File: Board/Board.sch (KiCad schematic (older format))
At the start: 55 parts, among them J1 Screw_Terminal_1x02, P1 USB_B, P2 CONN_01X05, P3 CONN_01X06, SW1 SW_SPST, SW2 SW_SPST, U1 MCP23016, U2 LM1117-3.3, U3 MCP9808, U4 ESP-12E

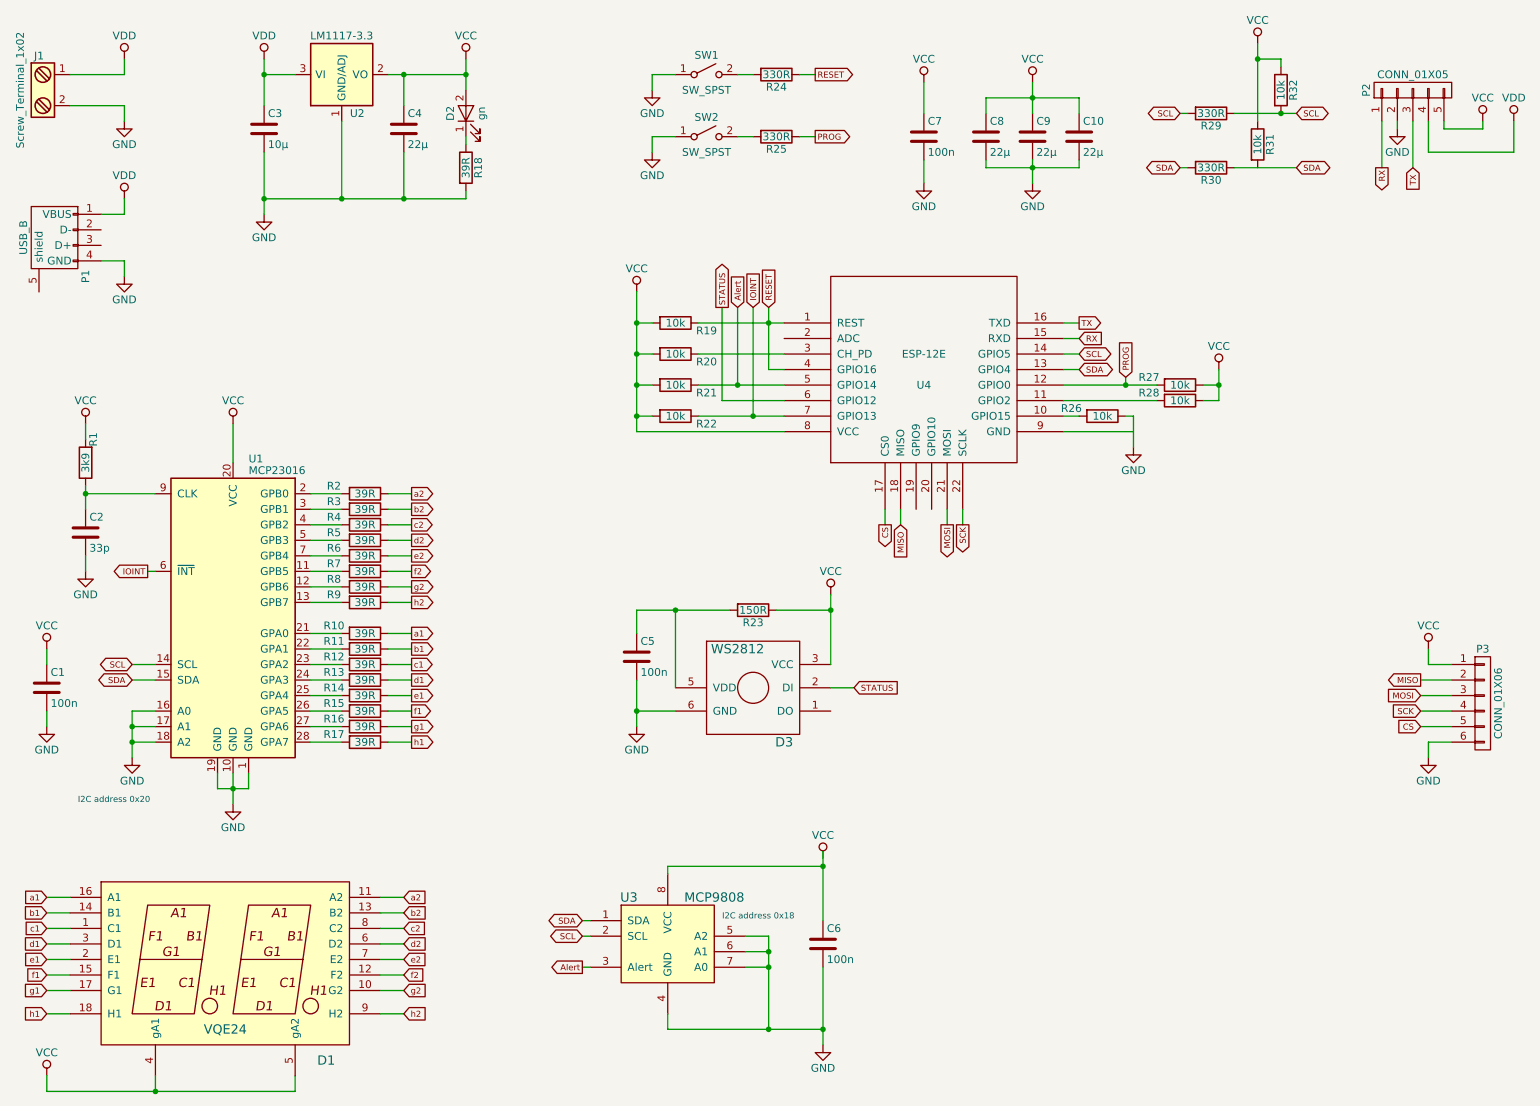
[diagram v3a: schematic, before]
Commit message: Layout for power and 7 segment display
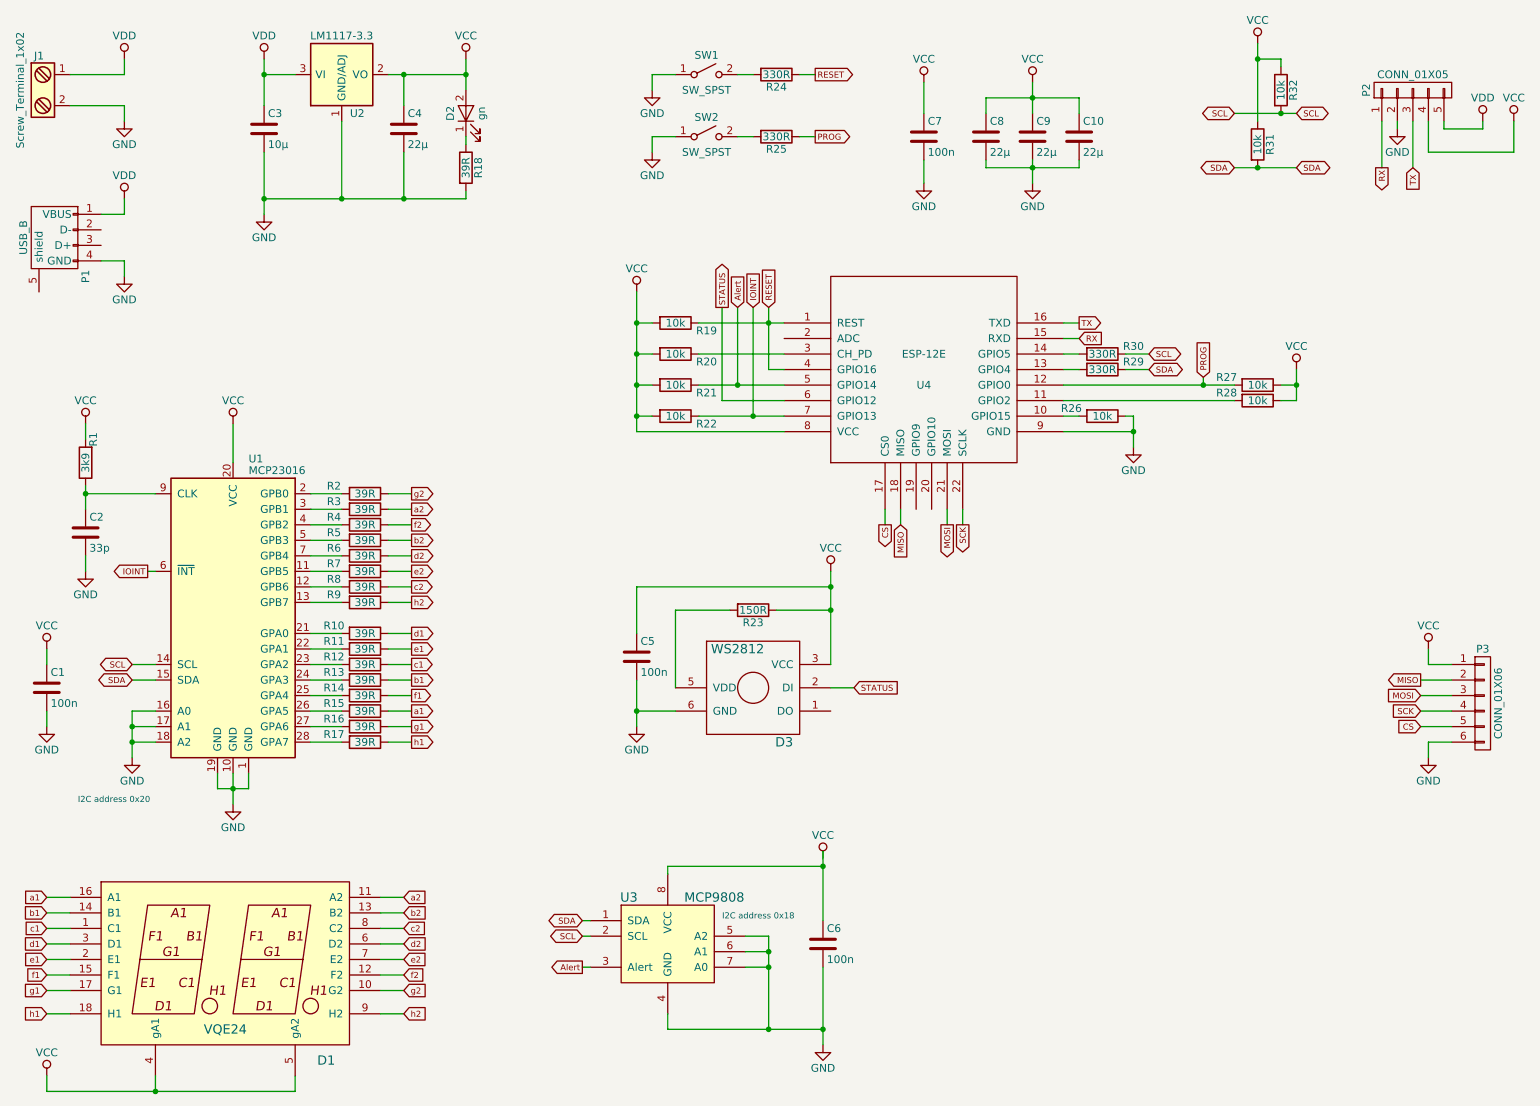
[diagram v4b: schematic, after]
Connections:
- net GND: now also U4.9 (GND)
- net SCL: now also R30.1; no longer R29.1, R29.2, U4.14 (GPIO5)
- net SDA: now also R29.1, R31.2; no longer R30.1, R30.2, U4.13 (GPIO4)
- net VCC: now also C5.1, P2.4 (P4); no longer P2.5 (P5)
- net VDD: now also P2.5 (P5); no longer P2.4 (P4)
- net a1: now also R15.1; no longer R10.1
- net a2: now also R3.1; no longer R2.1
- net b1: now also R13.1; no longer R11.1
- net b2: now also R5.1; no longer R3.1
- net c2: now also R8.1; no longer R4.1
- net d1: now also R10.1; no longer R13.1
- net d2: now also R6.1; no longer R5.1
- net e1: now also R11.1; no longer R14.1
- net e2: now also R7.1; no longer R6.1
- net f1: now also R14.1; no longer R15.1
- net f2: now also R4.1; no longer R7.1
- net g2: now also R2.1; no longer R8.1
- net at D3.5 (VDD), R23.2: no longer C5.1
- new net: R29.2, U4.13 (GPIO4)
- new net: R30.2, U4.14 (GPIO5)
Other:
- moved on the sheet: R27, R28, R29, R30

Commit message: Layout rev 1
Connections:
- net CS: now also P3.2 (P2); no longer P3.5 (P5)
- net MISO: now also P3.3 (P3); no longer P3.2 (P2)
- net MOSI: now also P3.4 (P4); no longer P3.3 (P3)
- net RX: now also P2.3 (P3); no longer P2.1 (P1)
- net SCK: now also P3.5 (P5); no longer P3.4 (P4)
- net TX: now also P2.1 (P1); no longer P2.3 (P3)
- net VCC: now also C6.1, U3.8 (VCC)
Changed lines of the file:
@@
 L VCC #PWR03
 U 1 1 5AD1E585
-P 6150 6050
-F 0 "#PWR03" H 6150 5900 50  0001 C CNN
-F 1 "VCC" H 6150 6200 50  0000 C CNN
-F 2 "" H 6150 6050 50  0000 C CNN
-F 3 "" H 6150 6050 50  0000 C CNN
-	1    6150 6050
+P 6150 6000
+F 0 "#PWR03" H 6150 5850 50  0001 C CNN
+F 1 "VCC" H 6150 6150 50  0000 C CNN
+F 2 "" H 6150 6000 50  0000 C CNN
+F 3 "" H 6150 6000 50  0000 C CNN
+	1    6150 6000
 	1    0    0    -1
 $EndComp
@@
 Wire Wire Line
 	5350 3000 5900 3000
-Text GLabel 9750 1600 3    39   Output ~ 0
+Text GLabel 9950 1600 3    39   Output ~ 0
 RX
 Text GLabel 7800 2700 2    39   Input ~ 0
@@
 Text GLabel 7800 2600 2    39   Output ~ 0
 TX
-Text GLabel 9950 1600 3    39   Input ~ 0
+Text GLabel 9750 1600 3    39   Input ~ 0
 TX
 Wire Wire Line
@@
 Wire Wire Line
 	10050 5300 10200 5300
-Text GLabel 10000 4900 0    39   Output ~ 0
+Text GLabel 10000 5000 0    39   Output ~ 0
 MISO
-Text GLabel 10000 5000 0    39   Input ~ 0
+Text GLabel 10000 5100 0    39   Input ~ 0
 MOSI
-Text GLabel 10000 5100 0    39   Input ~ 0
+Text GLabel 10000 5200 0    39   Input ~ 0
 SCK
 Wire Wire Line
@@
 	1    0    0    -1
 $EndComp
-Text GLabel 10000 5200 0    39   Input ~ 0
+Text GLabel 10000 4900 0    39   Input ~ 0
 CS
 Wire Wire Line

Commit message: Final Rev 1
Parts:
- removed C7: 100n, Capacitors_SMD:C_0603_HandSoldering, symbol C
- renumbered C10 to C7
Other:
- moved on the sheet: C7, C8, C9
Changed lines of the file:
@@
 L C C8
 U 1 1 5AD74D33
-P 7200 1400
-F 0 "C8" H 7225 1500 50  0000 L CNN
-F 1 "22µ" H 7225 1300 50  0000 L CNN
-F 2 "Capacitors_SMD:C_1206_HandSoldering" H 7238 1250 50  0001 C CNN
-F 3 "" H 7200 1400 50  0000 C CNN
-	1    7200 1400
-	1    0    0    -1
-$EndComp
-$Comp
-L C C9
-U 1 1 5AD7515D
 P 7500 1400
-F 0 "C9" H 7525 1500 50  0000 L CNN
+F 0 "C8" H 7525 1500 50  0000 L CNN
 F 1 "22µ" H 7525 1300 50  0000 L CNN
 F 2 "Capacitors_SMD:C_1206_HandSoldering" H 7538 1250 50  0001 C CNN
@@
 $EndComp
 $Comp
-L C C10
-U 1 1 5AD7521C
+L C C9
+U 1 1 5AD7515D
 P 7800 1400
-F 0 "C10" H 7825 1500 50  0000 L CNN
+F 0 "C9" H 7825 1500 50  0000 L CNN
 F 1 "22µ" H 7825 1300 50  0000 L CNN
 F 2 "Capacitors_SMD:C_1206_HandSoldering" H 7838 1250 50  0001 C CNN
 F 3 "" H 7800 1400 50  0000 C CNN
 	1    7800 1400
+	1    0    0    -1
+$EndComp
+$Comp
+L C C7
+U 1 1 5AD7521C
+P 7200 1400
+F 0 "C7" H 7225 1500 50  0000 L CNN
+F 1 "22µ" H 7225 1300 50  0000 L CNN
+F 2 "Capacitors_SMD:C_1206_HandSoldering" H 7238 1250 50  0001 C CNN
+F 3 "" H 7200 1400 50  0000 C CNN
+	1    7200 1400
 	1    0    0    -1
 $EndComp
@@
 Wire Wire Line
 	5500 3100 5900 3100
-$Comp
-L C C7
-U 1 1 5AD7760E
-P 6800 1400
-F 0 "C7" H 6825 1500 50  0000 L CNN
-F 1 "100n" H 6825 1300 50  0000 L CNN
-F 2 "Capacitors_SMD:C_0603_HandSoldering" H 6838 1250 50  0001 C CNN
-F 3 "" H 6800 1400 50  0000 C CNN
-	1    6800 1400
-	1    0    0    -1
-$EndComp
-Wire Wire Line
-	6800 1250 6800 1050
-Wire Wire Line
-	6800 1550 6800 1700
 Wire Wire Line
 	7500 1050 7500 1250
@@
 	1    0    0    -1
 $EndComp
-$Comp
-L GND #PWR031
-U 1 1 5AD7BB2C
-P 6800 1700
-F 0 "#PWR031" H 6800 1450 50  0001 C CNN
-F 1 "GND" H 6800 1550 50  0000 C CNN
-F 2 "" H 6800 1700 50  0000 C CNN
-F 3 "" H 6800 1700 50  0000 C CNN
-	1    6800 1700
-	1    0    0    -1
-$EndComp
-$Comp
-L VCC #PWR032
-U 1 1 5AD7BCE7
-P 6800 1050
-F 0 "#PWR032" H 6800 900 50  0001 C CNN
-F 1 "VCC" H 6800 1200 50  0000 C CNN
-F 2 "" H 6800 1050 50  0000 C CNN
-F 3 "" H 6800 1050 50  0000 C CNN
-	1    6800 1050
-	1    0    0    -1
-$EndComp
 Wire Wire Line
 	5050 2600 4950 2600
 $Comp
-L GND #PWR033
+L GND #PWR031
 U 1 1 5AD82799
 P 10050 5400
-F 0 "#PWR033" H 10050 5150 50  0001 C CNN
+F 0 "#PWR031" H 10050 5150 50  0001 C CNN
 F 1 "GND" H 10050 5250 50  0000 C CNN
 F 2 "" H 10050 5400 50  0000 C CNN
@@
 $EndComp
 $Comp
-L VCC #PWR034
+L VCC #PWR032
 U 1 1 5AD8279F
 P 10050 4700
-F 0 "#PWR034" H 10050 4550 50  0001 C CNN
+F 0 "#PWR032" H 10050 4550 50  0001 C CNN
 F 1 "VCC" H 10050 4850 50  0000 C CNN
 F 2 "" H 10050 4700 50  0000 C CNN

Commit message: Fix footprint for U1
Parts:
- U1: footprint SMD_Packages:SOIC-28 -> Housings_SOIC:SOIC-28W_7.5x17.9mm_Pitch1.27mm
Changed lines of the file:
@@
 F 0 "U1" H 2250 5525 50  0000 R CNN
 F 1 "MCP23016" H 2250 5450 50  0000 R CNN
-F 2 "SMD_Packages:SOIC-28" H 2500 3550 50  0001 L CNN
+F 2 "Housings_SOIC:SOIC-28W_7.5x17.9mm_Pitch1.27mm" H 2500 3550 50  0001 L CNN
 F 3 "" H 2600 5500 50  0001 C CNN
 	1    2350 4500

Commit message: Board Revision 3: Thermal relief for the temp sensor
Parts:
- removed C8, C9: 22µ, Capacitors_SMD:C_1206_HandSoldering, symbol C
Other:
- moved on the sheet: C7
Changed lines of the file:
@@
 Wire Wire Line
 	4950 2400 4950 3300
-Wire Wire Line
-	7200 1150 7200 1250
 Connection ~ 4950 2800
 Text GLabel 8600 2950 1    39   Input ~ 0
@@
 $EndComp
 Wire Wire Line
-	7200 1550 7200 1600
-Wire Wire Line
 	3850 1800 3850 1750
 Text GLabel 6100 1000 2    39   Output ~ 0
@@
 Connection ~ 5600 3000
 $Comp
-L C C8
-U 1 1 5AD74D33
+L C C7
+U 1 1 5AD7521C
 P 7500 1400
-F 0 "C8" H 7525 1500 50  0000 L CNN
+F 0 "C7" H 7525 1500 50  0000 L CNN
 F 1 "22µ" H 7525 1300 50  0000 L CNN
 F 2 "Capacitors_SMD:C_1206_HandSoldering" H 7538 1250 50  0001 C CNN
@@
 	1    0    0    -1
 $EndComp
-$Comp
-L C C9
-U 1 1 5AD7515D
-P 7800 1400
-F 0 "C9" H 7825 1500 50  0000 L CNN
-F 1 "22µ" H 7825 1300 50  0000 L CNN
-F 2 "Capacitors_SMD:C_1206_HandSoldering" H 7838 1250 50  0001 C CNN
-F 3 "" H 7800 1400 50  0000 C CNN
-	1    7800 1400
-	1    0    0    -1
-$EndComp
-$Comp
-L C C7
-U 1 1 5AD7521C
-P 7200 1400
-F 0 "C7" H 7225 1500 50  0000 L CNN
-F 1 "22µ" H 7225 1300 50  0000 L CNN
-F 2 "Capacitors_SMD:C_1206_HandSoldering" H 7238 1250 50  0001 C CNN
-F 3 "" H 7200 1400 50  0000 C CNN
-	1    7200 1400
-	1    0    0    -1
-$EndComp
 Wire Wire Line
 	5500 3100 5500 2500
@@
 	7500 1050 7500 1250
 Wire Wire Line
-	7800 1150 7800 1250
-Wire Wire Line
-	7200 1600 7800 1600
-Wire Wire Line
-	7800 1600 7800 1550
-Wire Wire Line
 	7500 1550 7500 1700
-Connection ~ 7500 1600
-Wire Wire Line
-	7200 1150 7800 1150
-Connection ~ 7500 1150
 $Comp
 L VCC #PWR030
